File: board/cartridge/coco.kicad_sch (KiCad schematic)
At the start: 21 parts, among them P1 Card Edge, U2 RP2350B, Y1 ABM8-272-T3

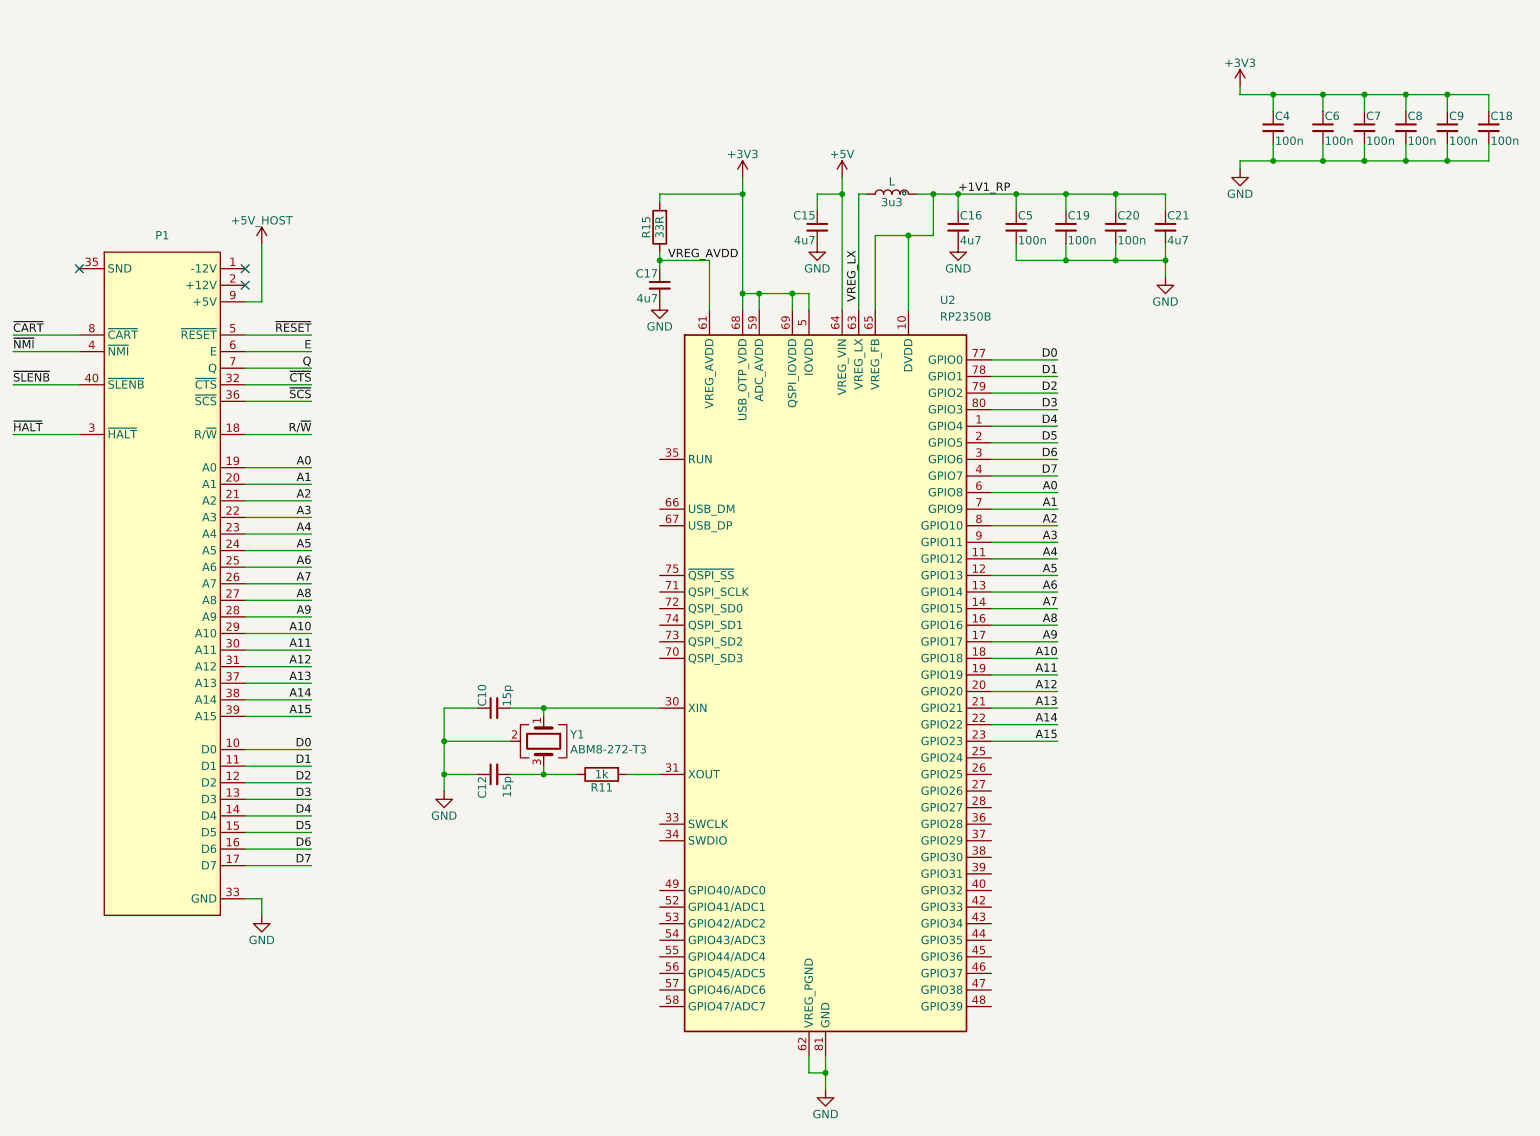
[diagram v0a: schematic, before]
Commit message: Route most of the RP2350.
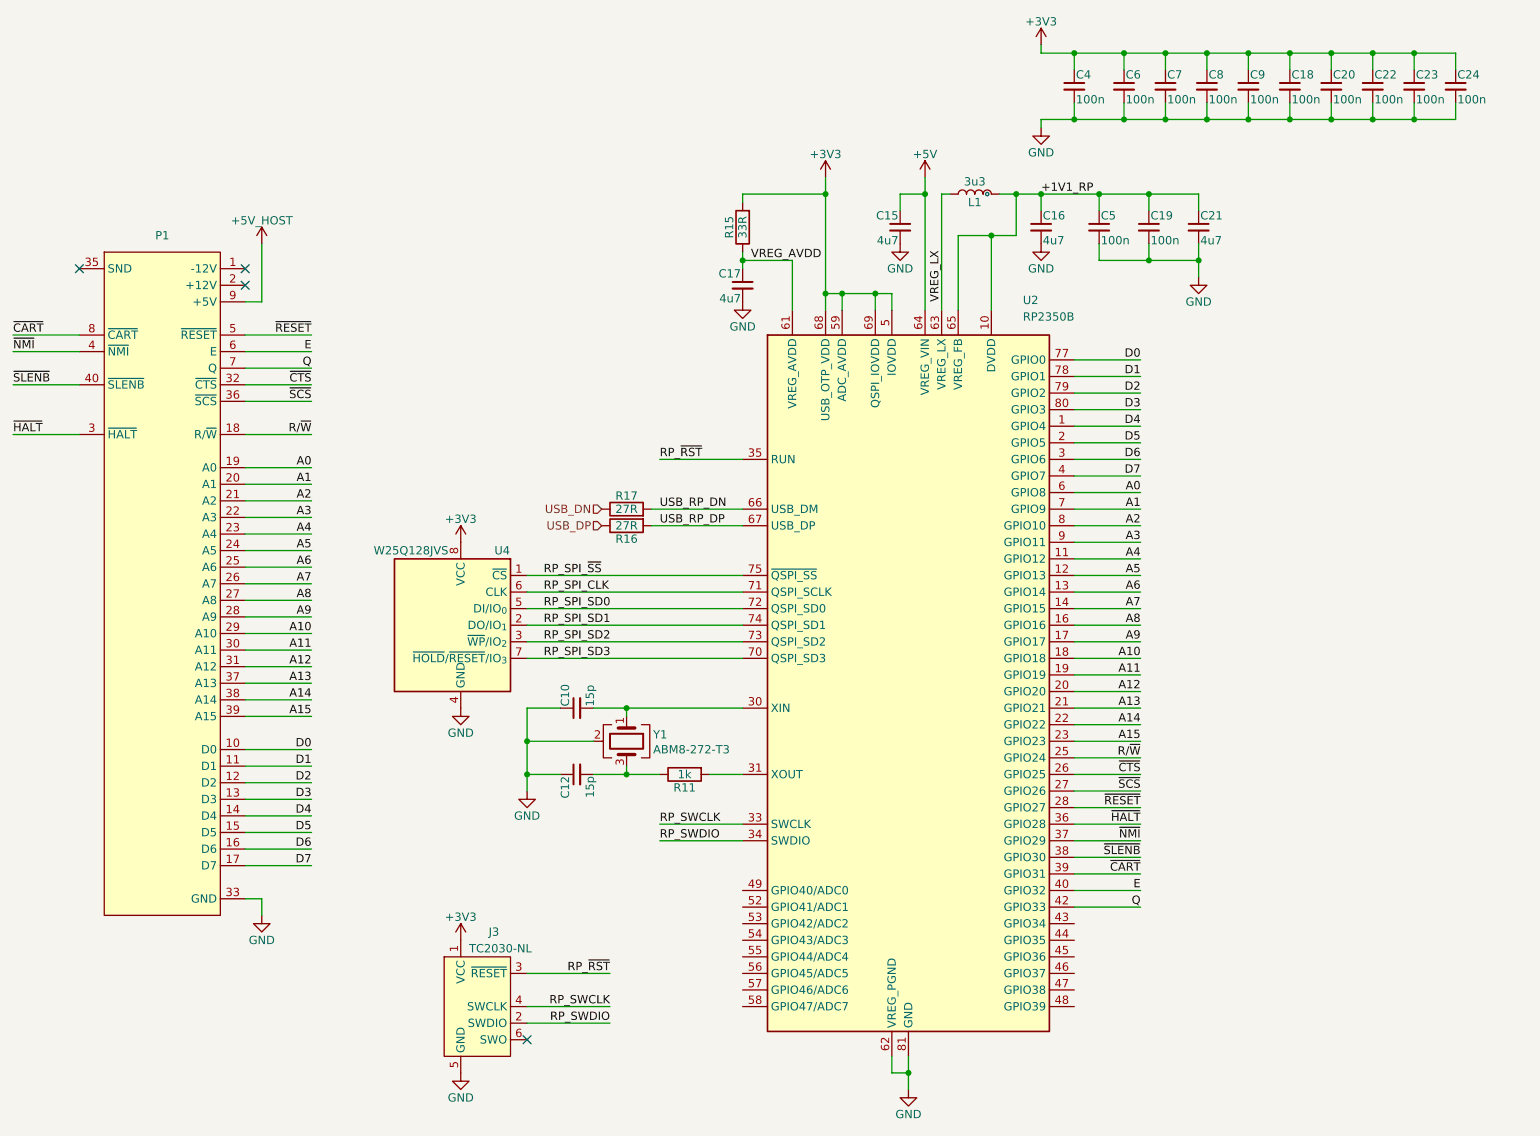
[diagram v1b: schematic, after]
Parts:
- added C22, C23, C24: 100n, Capacitor_SMD:C_0402_1005Metric, symbol Device:C_Small
- added J3: TC2030-NL, Connector:Tag-Connect_TC2030-IDC-NL_2x03_P1.27mm_Vertical, symbol Connector:Conn_ARM_SWD_TagConnect_TC2030-NL
- added R16, R17: 27R, Resistor_SMD:R_0402_1005Metric, symbol Device:R
- added U4: W25Q128JVS, Package_SO:SOIC-8_5.3x5.3mm_P1.27mm, symbol Memory_Flash:W25Q128JVS
- L1: renamed from 3u3; value L -> 3u3
- U2: footprint 0Project:QFN-80-1EP_10x10mm_P0.4mm_EP3.4x3.4mm_ThermalVias -> 0Project:RP2350-QFN-80-1EP_10x10_P0.4mm_EP3.4x3.4mm_ThermalVias
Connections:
- net +1V1_RP: no longer C20.1
- net +3V3: now also C20.1, C22.1, C23.1, C24.1, J3.1 (VCC), U4.8 (VCC)
- net E: now also U2.40 (GPIO32)
- net GND: now also C22.2, C23.2, C24.2, J3.5 (GND), U4.4 (GND)
- net Q: now also U2.42 (GPIO33)
- net R/~{W}: now also U2.25 (GPIO24)
- net ~{CART}: now also U2.39 (GPIO31)
- net ~{CTS}: now also U2.26 (GPIO25)
- net ~{HALT}: now also U2.36 (GPIO28)
- net ~{NMI}: now also U2.37 (GPIO29)
- net ~{RESET}: now also U2.28 (GPIO27)
- net ~{SCS}: now also U2.27 (GPIO26)
- net ~{SLENB}: now also U2.38 (GPIO30)
- net RP_SWCLK: now reaches U2.33 (SWCLK)
- net RP_SWCLK: now also J3.4 (SWCLK)
- net RP_SWDIO: now reaches U2.34 (SWDIO)
- net RP_SWDIO: now also J3.2 (SWDIO)
- net RP_~{RST}: now reaches U2.35 (RUN)
- net RP_~{RST}: now also J3.3 (~{RESET})
- net USB_RP_DN: now reaches U2.66 (USB_DM)
- net USB_RP_DN: now also R17.2
- net USB_RP_DP: now reaches U2.67 (USB_DP)
- net USB_RP_DP: now also R16.2
- net RP_SPI_SD3: now reaches U2.70 (QSPI_SD3)
- net RP_SPI_SD3: now also U4.7 (~{HOLD}/~{RESET}/IO_{3})
- net RP_SPI_CLK: now reaches U2.71 (QSPI_SCLK)
- net RP_SPI_CLK: now also U4.6 (CLK)
- net RP_SPI_SD0: now reaches U2.72 (QSPI_SD0)
- net RP_SPI_SD0: now also U4.5 (DI/IO_{0})
- net RP_SPI_SD2: now reaches U2.73 (QSPI_SD2)
- net RP_SPI_SD2: now also U4.3 (~{WP}/IO_{2})
- net RP_SPI_SD1: now reaches U2.74 (QSPI_SD1)
- net RP_SPI_SD1: now also U4.2 (DO/IO_{1})
- net RP_SPI_~{SS}: now reaches U2.75 (~{QSPI_SS})
- net RP_SPI_~{SS}: now also U4.1 (~{CS})
- new net USB_DN: R17.1
- new net USB_DP: R16.1
- no-connect marks 3 -> 4
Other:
- moved on the sheet: C10, C12, C15, C16, C17, C18, C19, C21, C4, C5, C6, C7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
